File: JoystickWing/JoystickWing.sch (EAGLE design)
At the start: 19 parts, among them J1 5747844-4

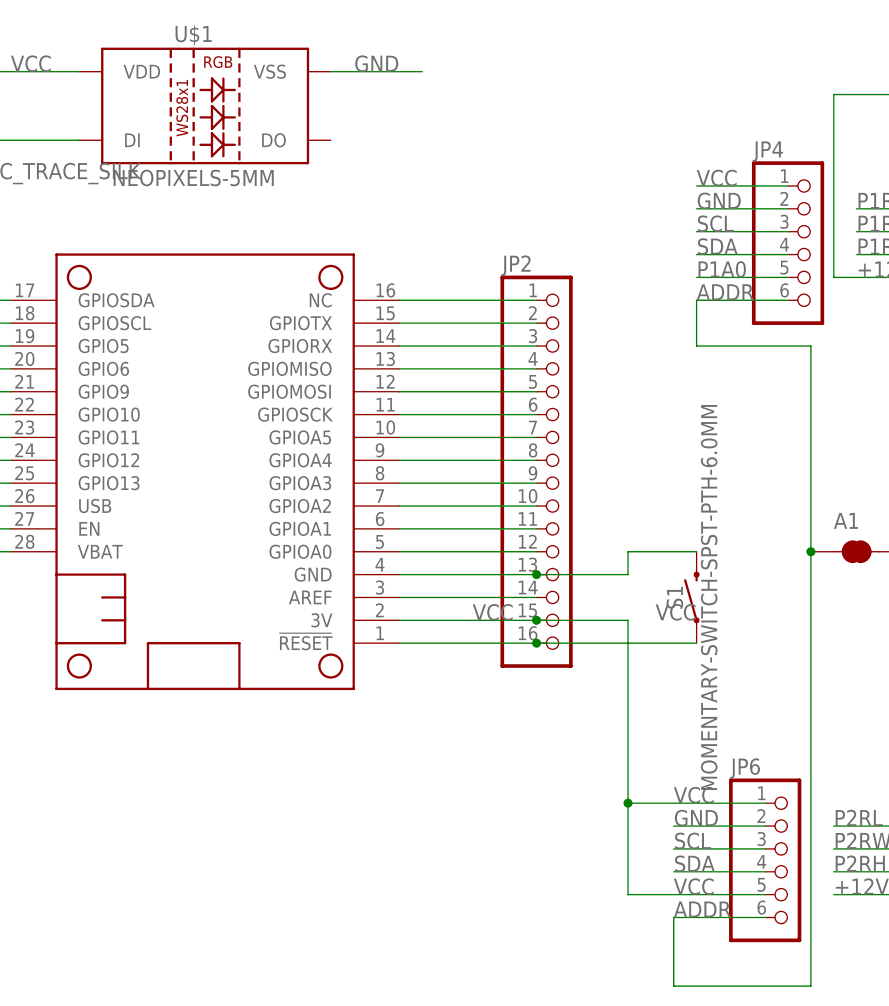
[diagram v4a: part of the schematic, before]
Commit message: Added the missing Neopixel led pads and updated the switch to DTS-3: 3.5x6mm style switch.
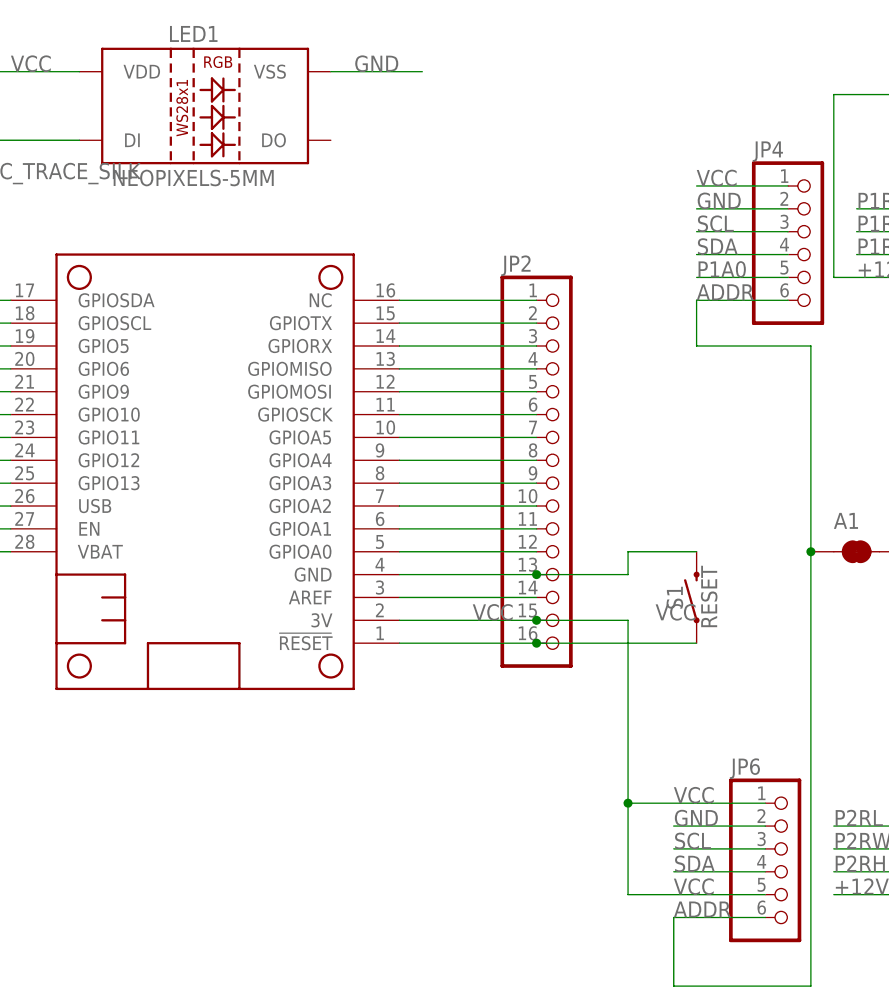
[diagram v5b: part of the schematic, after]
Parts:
- S1: value MOMENTARY-SWITCH-SPST-PTH-6.0MM -> RESET; device SparkFun-Switches:MOMENTARY-SWITCH-SPST-PTH-6.0MM -> milador:SWITCH_DTS-3
- renumbered U$1 to LED1
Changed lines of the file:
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@@
 <?xml version="1.0" encoding="utf-8"?>
 <!DOCTYPE eagle SYSTEM "eagle.dtd">
-<eagle version="9.2.2">
+<eagle version="9.4.2">
 <drawing>
 <settings>
@@
 <layers>
 <layer number="1" name="Top" color="4" fill="1" visible="no" active="no"/>
+<layer number="2" name="Route2" color="1" fill="3" visible="no" active="no"/>
+<layer number="3" name="Route3" color="4" fill="3" visible="no" active="no"/>
+<layer number="4" name="Route4" color="1" fill="4" visible="no" active="no"/>
+<layer number="5" name="Route5" color="4" fill="4" visible="no" active="no"/>
+<layer number="6" name="Route6" color="1" fill="8" visible="no" active="no"/>
+<layer number="7" name="Route7" color="4" fill="8" visible="no" active="no"/>
+<layer number="8" name="Route8" color="1" fill="2" visible="no" active="no"/>
+<layer number="9" name="Route9" color="4" fill="2" visible="no" active="no"/>
+<layer number="10" name="Route10" color="1" fill="7" visible="no" active="no"/>
+<layer number="11" name="Route11" color="4" fill="7" visible="no" active="no"/>
+<layer number="12" name="Route12" color="1" fill="5" visible="no" active="no"/>
+<layer number="13" name="Route13" color="4" fill="5" visible="no" active="no"/>
+<layer number="14" name="Route14" color="1" fill="6" visible="no" active="no"/>
+<layer number="15" name="Route15" color="4" fill="6" visible="no" active="no"/>
 <layer number="16" name="Bottom" color="1" fill="1" visible="no" active="no"/>
 <layer number="17" name="Pads" color="2" fill="1" visible="no" active="no"/>
@@
 <part name="JP1" library="adafruit" library_urn="urn:adsk.eagle:library:420" deviceset="PINHD-1X12" device="-CB" package3d_urn="urn:adsk.eagle:package:6240772/1"/>
 <part name="JP2" library="pinhead" library_urn="urn:adsk.eagle:library:325" deviceset="PINHD-1X16" device="" package3d_urn="urn:adsk.eagle:package:22432/2"/>
-<part name="U$1" library="milador" deviceset="NEOPIXELS-5MM" device="" package3d_urn="urn:adsk.eagle:package:6677832/4"/>
+<part name="LED1" library="milador" library_urn="urn:adsk.eagle:library:12595918" deviceset="NEOPIXELS-5MM" device="" package3d_urn="urn:adsk.eagle:package:6677832/5"/>
 <part name="JP7" library="SparkFun-Jumpers" deviceset="JUMPER-SMT_2_NC_TRACE" device="_SILK"/>
 <part name="NEOPIN" library="wirepad" library_urn="urn:adsk.eagle:library:412" deviceset="2,54/1,1" device="" package3d_urn="urn:adsk.eagle:package:30836/1"/>
-<part name="S1" library="SparkFun-Switches" library_urn="urn:adsk.eagle:library:535" deviceset="MOMENTARY-SWITCH-SPST" device="-PTH-6.0MM" package3d_urn="urn:adsk.eagle:package:40163/1"/>
+<part name="S1" library="milador" library_urn="urn:adsk.eagle:library:12595918" deviceset="SWITCH_DTS-3" device="" value="RESET"/>
 <part name="A1" library="SparkFun-Jumpers" deviceset="JUMPER-SMT_2_NC_TRACE" device="_SILK"/>
 </parts>
@@
 <attribute name="VALUE" x="-44.45" y="25.4" size="1.778" layer="96"/>
 </instance>
-<instance part="U$1" gate="G$1" x="-76.2" y="88.9" smashed="yes">
+<instance part="LED1" gate="G$1" x="-76.2" y="88.9" smashed="yes">
 <attribute name="NAME" x="-78.74" y="97.282" size="1.778" layer="95" font="vector" align="bottom-center"/>
 <attribute name="VALUE" x="-78.74" y="81.28" size="1.778" layer="95" font="vector" align="bottom-center"/>
@@
 </segment>
 <segment>
-<pinref part="U$1" gate="G$1" pin="VSS"/>
+<pinref part="LED1" gate="G$1" pin="VSS"/>
 <wire x1="-63.5" y1="93.98" x2="-53.34" y2="93.98" width="0.1524" layer="91"/>
 <label x="-55.88" y="93.98" size="1.778" layer="95" align="bottom-right"/>
@@
 </segment>
 <segment>
-<pinref part="U$1" gate="G$1" pin="VDD"/>
+<pinref part="LED1" gate="G$1" pin="VDD"/>
 <wire x1="-91.44" y1="93.98" x2="-101.6" y2="93.98" width="0.1524" layer="91"/>
 <label x="-99.06" y="93.98" size="1.778" layer="95"/>
@@
 <net name="N$25" class="0">
 <segment>
-<pinref part="U$1" gate="G$1" pin="DI"/>
+<pinref part="LED1" gate="G$1" pin="DI"/>
 <pinref part="NEOPIN" gate="1" pin="P"/>
 <wire x1="-91.44" y1="86.36" x2="-104.14" y2="86.36" width="0.1524" layer="91"/>

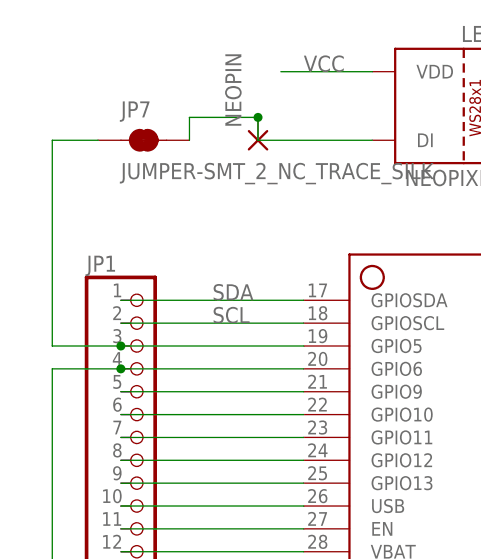
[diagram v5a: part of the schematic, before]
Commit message: Cleaning up for manu
Added restriction around traces for the jumpers
Added text and a place for the PCBWay product num
Replaced pins to be consistent
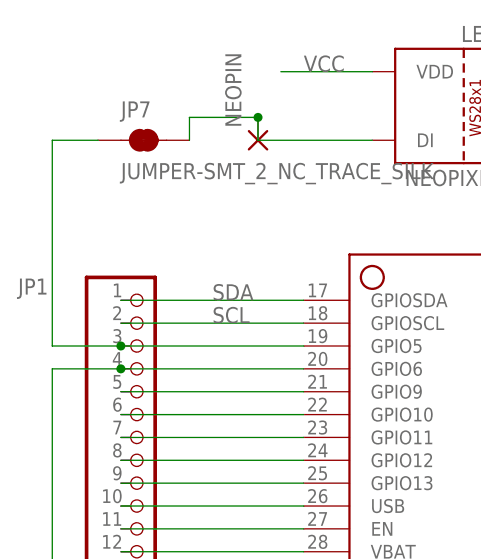
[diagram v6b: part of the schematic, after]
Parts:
- JP1: device adafruit:PINHD-1X12-CB -> adafruit:PINHD-1X12
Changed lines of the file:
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@@
 <?xml version="1.0" encoding="utf-8"?>
 <!DOCTYPE eagle SYSTEM "eagle.dtd">
-<eagle version="9.4.2">
+<eagle version="9.2.2">
 <drawing>
 <settings>
@@
 <grid distance="0.1" unitdist="inch" unit="inch" style="lines" multiple="1" display="no" altdistance="0.01" altunitdist="inch" altunit="inch"/>
 <layers>
-<layer number="1" name="Top" color="4" fill="1" visible="no" active="no"/>
-<layer number="2" name="Route2" color="1" fill="3" visible="no" active="no"/>
-<layer number="3" name="Route3" color="4" fill="3" visible="no" active="no"/>
-<layer number="4" name="Route4" color="1" fill="4" visible="no" active="no"/>
-<layer number="5" name="Route5" color="4" fill="4" visible="no" active="no"/>
-<layer number="6" name="Route6" color="1" fill="8" visible="no" active="no"/>
-<layer number="7" name="Route7" color="4" fill="8" visible="no" active="no"/>
-<layer number="8" name="Route8" color="1" fill="2" visible="no" active="no"/>
-<layer number="9" name="Route9" color="4" fill="2" visible="no" active="no"/>
-<layer number="10" name="Route10" color="1" fill="7" visible="no" active="no"/>
-<layer number="11" name="Route11" color="4" fill="7" visible="no" active="no"/>
-<layer number="12" name="Route12" color="1" fill="5" visible="no" active="no"/>
-<layer number="13" name="Route13" color="4" fill="5" visible="no" active="no"/>
-<layer number="14" name="Route14" color="1" fill="6" visible="no" active="no"/>
-<layer number="15" name="Route15" color="4" fill="6" visible="no" active="no"/>
-<layer number="16" name="Bottom" color="1" fill="1" visible="no" active="no"/>
-<layer number="17" name="Pads" color="2" fill="1" visible="no" active="no"/>
-<layer number="18" name="Vias" color="2" fill="1" visible="no" active="no"/>
-<layer number="19" name="Unrouted" color="6" fill="1" visible="no" active="no"/>
-<layer number="20" name="Dimension" color="24" fill="1" visible="no" active="no"/>
-<layer number="21" name="tPlace" color="7" fill="1" visible="no" active="no"/>
-<layer number="22" name="bPlace" color="7" fill="1" visible="no" active="no"/>
-<layer number="23" name="tOrigins" color="15" fill="1" visible="no" active="no"/>
-<layer number="24" name="bOrigins" color="15" fill="1" visible="no" active="no"/>
-<layer number="25" name="tNames" color="7" fill="1" visible="no" active="no"/>
-<layer number="26" name="bNames" color="7" fill="1" visible="no" active="no"/>
-<layer number="27" name="tValues" color="7" fill="1" visible="no" active="no"/>
-<layer number="28" name="bValues" color="7" fill="1" visible="no" active="no"/>
+<layer number="1" name="Top" color="4" fill="1" visible="yes" active="no"/>
+<layer number="2" name="Route2" color="1" fill="3" visible="yes" active="no"/>
+<layer number="3" name="Route3" color="4" fill="3" visible="yes" active="no"/>
+<layer number="4" name="Route4" color="1" fill="4" visible="yes" active="no"/>
+<layer number="5" name="Route5" color="4" fill="4" visible="yes" active="no"/>
+<layer number="6" name="Route6" color="1" fill="8" visible="yes" active="no"/>
+<layer number="7" name="Route7" color="4" fill="8" visible="yes" active="no"/>
+<layer number="8" name="Route8" color="1" fill="2" visible="yes" active="no"/>
+<layer number="9" name="Route9" color="4" fill="2" visible="yes" active="no"/>
+<layer number="10" name="Route10" color="1" fill="7" visible="yes" active="no"/>
+<layer number="11" name="Route11" color="4" fill="7" visible="yes" active="no"/>
+<layer number="12" name="Route12" color="1" fill="5" visible="yes" active="no"/>
+<layer number="13" name="Route13" color="4" fill="5" visible="yes" active="no"/>
+<layer number="14" name="Route14" color="1" fill="6" visible="yes" active="no"/>
+<layer number="15" name="Route15" color="4" fill="6" visible="yes" active="no"/>
+<layer number="16" name="Bottom" color="1" fill="1" visible="yes" active="no"/>
+<layer number="17" name="Pads" color="2" fill="1" visible="yes" active="no"/>
+<layer number="18" name="Vias" color="2" fill="1" visible="yes" active="no"/>
+<layer number="19" name="Unrouted" color="6" fill="1" visible="yes" active="no"/>
+<layer number="20" name="Dimension" color="24" fill="1" visible="yes" active="no"/>
+<layer number="21" name="tPlace" color="7" fill="1" visible="yes" active="no"/>
+<layer number="22" name="bPlace" color="7" fill="1" visible="yes" active="no"/>
+<layer number="23" name="tOrigins" color="15" fill="1" visible="yes" active="no"/>
+<layer number="24" name="bOrigins" color="15" fill="1" visible="yes" active="no"/>
+<layer number="25" name="tNames" color="7" fill="1" visible="yes" active="no"/>
+<layer number="26" name="bNames" color="7" fill="1" visible="yes" active="no"/>
+<layer number="27" name="tValues" color="7" fill="1" visible="yes" active="no"/>
+<layer number="28" name="bValues" color="7" fill="1" visible="yes" active="no"/>
 <layer number="29" name="tStop" color="7" fill="3" visible="no" active="no"/>
 <layer number="30" name="bStop" color="7" fill="6" visible="no" active="no"/>
@@
 <layer number="35" name="tGlue" color="7" fill="4" visible="no" active="no"/>
 <layer number="36" name="bGlue" color="7" fill="5" visible="no" active="no"/>
-<layer number="37" name="tTest" color="7" fill="1" visible="no" active="no"/>
-<layer number="38" name="bTest" color="7" fill="1" visible="no" active="no"/>
+<layer number="37" name="tTest" color="7" fill="1" visible="yes" active="no"/>
+<layer number="38" name="bTest" color="7" fill="1" visible="yes" active="no"/>
 <layer number="39" name="tKeepout" color="4" fill="11" visible="no" active="no"/>
 <layer number="40" name="bKeepout" color="1" fill="11" visible="no" active="no"/>
@@
 <layer number="44" name="Drills" color="7" fill="1" visible="no" active="no"/>
 <layer number="45" name="Holes" color="7" fill="1" visible="no" active="no"/>
-<layer number="46" name="Milling" color="3" fill="1" visible="no" active="no"/>
-<layer number="47" name="Measures" color="7" fill="1" visible="no" active="no"/>
-<layer number="48" name="Document" color="7" fill="1" visible="no" active="no"/>
-<layer number="49" name="Reference" color="7" fill="1" visible="no" active="no"/>
-<layer number="50" name="dxf" color="7" fill="1" visible="no" active="no"/>
-<layer number="51" name="tDocu" color="7" fill="1" visible="no" active="no"/>
-<layer number="52" name="bDocu" color="7" fill="1" visible="no" active="no"/>
-<layer number="53" name="tGND_GNDA" color="7" fill="9" visible="no" active="no"/>
-<layer number="54" name="bGND_GNDA" color="1" fill="9" visible="no" active="no"/>
-<layer number="56" name="wert" color="7" fill="1" visible="no" active="no"/>
-<layer number="57" name="tCAD" color="7" fill="1" visible="no" active="no"/>
-<layer number="58" name="bCAD" color="7" fill="1" visible="no" active="no"/>
-<layer number="59" name="tCarbon" color="7" fill="1" visible="no" active="no"/>
-<layer number="60" name="bCarbon" color="7" fill="1" visible="no" active="no"/>
-<layer number="61" name="stand" color="7" fill="1" visible="no" active="no"/>
+<layer number="46" name="Milling" color="3" fill="1" visible="yes" active="no"/>
+<layer number="47" name="Measures" color="7" fill="1" visible="yes" active="no"/>
+<layer number="48" name="Document" color="7" fill="1" visible="yes" active="no"/>
+<layer number="49" name="Reference" color="7" fill="1" visible="yes" active="no"/>
+<layer number="50" name="dxf" color="7" fill="1" visible="yes" active="no"/>
+<layer number="51" name="tDocu" color="7" fill="1" visible="yes" active="no"/>
+<layer number="52" name="bDocu" color="7" fill="1" visible="yes" active="no"/>
+<layer number="53" name="tGND_GNDA" color="7" fill="9" visible="yes" active="no"/>
+<layer number="54" name="bGND_GNDA" color="1" fill="9" visible="yes" active="no"/>
+<layer number="56" name="wert" color="7" fill="1" visible="yes" active="no"/>
+<layer number="57" name="tCAD" color="7" fill="1" visible="yes" active="no"/>
+<layer number="58" name="bCAD" color="7" fill="1" visible="yes" active="no"/>
+<layer number="59" name="tCarbon" color="7" fill="1" visible="yes" active="no"/>
+<layer number="60" name="bCarbon" color="7" fill="1" visible="yes" active="no"/>
+<layer number="61" name="stand" color="7" fill="1" visible="yes" active="no"/>
 <layer number="88" name="SimResults" color="9" fill="1" visible="yes" active="yes"/>
 <layer number="89" name="SimProbes" color="9" fill="1" visible="yes" active="yes"/>
@@
 <part name="JP5" library="microbuilder" deviceset="HEADER-1X4" device="ROUND"/>
 <part name="JP6" library="microbuilder" deviceset="HEADER-1X6" device="ROUND"/>
-<part name="JP1" library="adafruit" library_urn="urn:adsk.eagle:library:420" deviceset="PINHD-1X12" device="-CB" package3d_urn="urn:adsk.eagle:package:6240772/1"/>
+<part name="JP1" library="adafruit" library_urn="urn:adsk.eagle:library:420" deviceset="PINHD-1X12" device="" package3d_urn="urn:adsk.eagle:package:6240771/1"/>
 <part name="JP2" library="pinhead" library_urn="urn:adsk.eagle:library:325" deviceset="PINHD-1X16" device="" package3d_urn="urn:adsk.eagle:package:22432/2"/>
 <part name="LED1" library="milador" library_urn="urn:adsk.eagle:library:12595918" deviceset="NEOPIXELS-5MM" device="" package3d_urn="urn:adsk.eagle:package:6677832/5"/>
@@
 </instance>
 <instance part="JP1" gate="G$1" x="-116.84" y="55.88" smashed="yes">
-<attribute name="NAME" x="-123.19" y="71.755" size="1.778" layer="95"/>
+<attribute name="NAME" x="-130.81" y="69.215" size="1.778" layer="95"/>
 <attribute name="VALUE" x="-123.19" y="35.56" size="1.778" layer="96"/>
 </instance>
